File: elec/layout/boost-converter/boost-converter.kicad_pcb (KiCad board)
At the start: 2 copper layers, 14 parts

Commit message: build and re-link layouts
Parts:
- C7: value 4.7µF ±20% 6.3V X5R -> 4.7µF ±20% 10V X5R
- R1: value 10kΩ ±1% 62.5mW -> 10kΩ ±1% 100mW; footprint atopile:R0402-56259e -> atopile:R0603-ebcab9
- R2: value 180kΩ ±1% 62.5mW -> 180kΩ ±1% 100mW; footprint atopile:R0402-56259e -> atopile:R0603-ebcab9
- R3: value 2.7kΩ ±1% 62.5mW -> 2.49kΩ ±1% 62.5mW

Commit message: all modules building
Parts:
- C7: value 4.7µF ±20% 10V X5R -> 4.7µF ±20% 6.3V X5R
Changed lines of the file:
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@@
                     (size 1 1)
                     (thickness 0.15))))
-        (property "Value" "4.7µF ±20% 10V X5R"
+        (property "Value" "4.7µF ±20% 6.3V X5R"
             (at 0 4 90)
             (layer "F.Fab")
@@
                     (size 0.125 0.125)
                     (thickness 0.01875))))
-        (property "LCSC" "C23733"
+        (property "LCSC" "C307423"
             (at 0 0 90)
             (layer "User.9")
@@
                     (size 0.125 0.125)
                     (thickness 0.01875))))
-        (property "Partnumber" "CL05A475MP5NRNC"
+        (property "Partnumber" "CL05A475MQ5NRNC"
             (at 0 0 90)
             (layer "User.9")
@@
                     (size 0.125 0.125)
                     (thickness 0.01875))))
-        (property "JLCPCB description" "10V 4.7uF X5R ±20% 0402 Multilayer Ceramic Capacitors MLCC - SMD/SMT ROHS"
+        (property "JLCPCB description" "6.3V 4.7uF X5R ±20% 0402 Multilayer Ceramic Capacitors MLCC - SMD/SMT ROHS"
             (at 0 0 90)
             (layer "User.9")

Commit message: HIL Building
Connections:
- C2 pad 1: hv-1 -> hv
- C3 pad 1: hv-1 -> hv
- C4 pad 1: hv -> hv-1
- C5 pad 1: hv -> hv-1
- C6 pad 1: hv -> hv-1
- D1 pad 1: hv -> hv-1
- L1 pad 1: hv-1 -> hv
- R2 pad 1: hv -> hv-1
- U1 pad 2: hv-1 -> hv
- U1 pad 3: hv-1 -> hv
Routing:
- net hv-1: track 17.0 -> 14.5 mm, vias 5 -> 12
- net hv: track 14.5 -> 17.0 mm, vias 12 -> 5
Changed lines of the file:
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@@
     (net 2 "FB")
     (net 3 "ic.footprint.pins[5].net-net")
-    (net 4 "hv-1")
-    (net 5 "hv")
+    (net 4 "hv")
+    (net 5 "hv-1")
     (net 6 "net")
     (net 7 "SS")
@@
             (layers "F.Cu" "F.Paste" "F.Mask")
             (remove_unused_layers no)
-            (net 5 "hv")))
+            (net 5 "hv-1")))
     (footprint "atopile:R0603-ebcab9"
         (layer "F.Cu")
@@
             (layers "F.Cu" "F.Paste" "F.Mask")
             (remove_unused_layers no)
-            (net 4 "hv-1"))
+            (net 4 "hv"))
         (pad "2" smd rect
             (at 1 0 0)
@@
             (layers "F.Cu" "F.Paste" "F.Mask")
             (remove_unused_layers no)
-            (net 4 "hv-1"))
+            (net 4 "hv"))
         (pad "2" smd rect
             (at 1 0 0)
@@
             (layers "F.Cu" "F.Paste" "F.Mask")
             (remove_unused_layers no)
-            (net 5 "hv"))
+            (net 5 "hv-1"))
         (pad "2" smd rect
             (at 1 0 0)
@@
             (layers "F.Cu" "F.Paste" "F.Mask")
             (remove_unused_layers no)
-            (net 5 "hv"))
+            (net 5 "hv-1"))
         (pad "2" smd rect
             (at 1 0 0)
@@
                     (size 0.125 0.125)
                     (thickness 0.01875))))
-        (property "LCSC" "C137935"
+        (property "LCSC" "C25798"
             (at 0 0 90)
             (layer "User.9")
@@
                     (size 0.125 0.125)
                     (thickness 0.01875))))
-        (property "Partnumber" "RC0402FR-0775KL"
+        (property "Partnumber" "0402WGF7502TCE"
             (at 0 0 90)
             (layer "User.9")
@@
                     (size 0.125 0.125)
                     (thickness 0.01875))))
-        (property "Manufacturer" "YAGEO"
+        (property "Manufacturer" "UNI-ROYAL(Uniroyal Elec)"
             (at 0 0 90)
             (layer "User.9")
@@
             (layers "F.Cu" "F.Paste" "F.Mask")
             (remove_unused_layers no)
-            (net 4 "hv-1"))
+            (net 4 "hv"))
         (pad "3" smd rect
             (at 0.25 1.5 270)
@@
             (layers "F.Cu" "F.Paste" "F.Mask")
             (remove_unused_layers no)
-            (net 4 "hv-1"))
+            (net 4 "hv"))
         (pad "4" smd rect
             (at 0.75 1.5 270)
@@
             (layers "F.Cu" "F.Paste" "F.Mask")
             (remove_unused_layers no)
-            (net 5 "hv"))
+            (net 5 "hv-1"))
         (pad "2" smd rect
             (at 1 0 0)
@@
             (layers "F.Cu" "F.Paste" "F.Mask")
             (remove_unused_layers no)
-            (net 4 "hv-1"))
+            (net 4 "hv"))
         (pad "2" smd rect
             (at 2.91 0 90)
@@
             (layers "F.Cu" "F.Paste" "F.Mask")
             (remove_unused_layers no)
-            (net 5 "hv"))
+            (net 5 "hv-1"))
         (pad "2" smd rect
             (at 3.43 0 0)
@@
     (zone
         (net 5)
-        (net_name "hv")
+        (net_name "hv-1")
         (layers "F.Cu")
         (hatch edge 0.5)
@@
     (zone
         (net 5)
-        (net_name "hv")
+        (net_name "hv-1")
         (layers "F.Cu")
         (hatch edge 0.5)
@@
     (zone
         (net 4)
-        (net_name "hv-1")
+        (net_name "hv")
         (layers "F.Cu")
         (hatch edge 0.5)

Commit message: build with latest main
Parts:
- removed C1: 6.8nF ±10% 50V X7R, atopile:C0402-b3ef17
- removed C2, C3, C4, C5, C6: 10µF ±10% 25V X5R, atopile:C0805-3b2e55
- removed C7: 4.7µF ±20% 6.3V X5R, atopile:C0402-b3ef17
- removed D1: , atopile:SMC_L7.1-W6.2-LS8.1-RD-d9649d
- removed L1: , atopile:IND-SMD_L7.1-W6.6-48b69f
- removed R1: 10kΩ ±1% 100mW, atopile:R0603-ebcab9
- removed R2: 180kΩ ±1% 100mW, atopile:R0603-ebcab9
- removed R3: 2.49kΩ ±1% 62.5mW, atopile:R0402-56259e
- removed R4: 75kΩ ±1% 62.5mW, atopile:R0402-56259e
- removed U1: , atopile:VQFN-16_L3.0-W3.0-P0.50-BL-EP1.7-62c35a
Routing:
- net gnd: track 17.2 -> 0.00 mm, vias 19 -> 0
- net hv: track 17.0 -> 0.00 mm, vias 5 -> 0
- net hv-1: track 14.5 -> 0.00 mm, vias 12 -> 0
- net switching_node: track 13.2 -> 0.00 mm
- net FB: track 4.55 -> 0.00 mm
- net COMP: track 3.32 -> 0.00 mm
- net FREQ: track 2.01 -> 0.00 mm
- net net: track 1.30 -> 0.00 mm
- net SS: track 1.24 -> 0.00 mm
- removed copper zone on B.Cu, net gnd
- removed copper zone on F.Cu, net gnd
- removed copper zone on F.Cu, net hv
- removed copper zone on F.Cu, net hv-1
- removed copper zone on F.Cu, net switching_node

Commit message: building frozen
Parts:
- added C1: 6.8nF ±10% 50V X7R, atopile:C0402-b3ef17, F.Cu at (106.1, 57.8)
- added C2: 10µF ±10% 25V X5R, atopile:C0805-3b2e55, F.Cu at (101.9, 59.6)
- added C3: 10µF ±10% 25V X5R, atopile:C0805-3b2e55, F.Cu at (101.9, 57.6)
- added C4: 10µF ±10% 25V X5R, atopile:C0805-3b2e55, F.Cu at (104.2, 46.0)
- added C5: 10µF ±10% 25V X5R, atopile:C0805-3b2e55, F.Cu at (104.2, 48.0)
- added C6: 10µF ±10% 25V X5R, atopile:C0805-3b2e55, F.Cu at (104.2, 50.0)
- added C7: 4.7µF ±20% 6.3V X5R, atopile:C0402-b3ef17, F.Cu at (100.5, 54.8)
- added D1: , atopile:SMC_L7.1-W6.2-LS8.1-RD-d9649d, F.Cu at (97.0, 48.3)
- added L1: , atopile:IND-SMD_L7.1-W6.6-48b69f, F.Cu at (96.4, 55.7)
- added R1: 10kΩ ±1% 100mW, atopile:R0603-ebcab9, F.Cu at (107.0, 52.9)
- added R2: 180kΩ ±1% 100mW, atopile:R0603-ebcab9, F.Cu at (106.3, 55.2)
- added R3: 2.49kΩ ±1% 62.5mW, atopile:R0402-56259e, F.Cu at (106.2, 56.5)
- added R4: 75kΩ ±1% 62.5mW, atopile:R0402-56259e, F.Cu at (105.8, 52.9)
- added U1: , atopile:VQFN-16_L3.0-W3.0-P0.50-BL-EP1.7-62c35a, F.Cu at (103.1, 53.8)
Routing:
- net gnd: track 0.00 -> 17.2 mm, vias 0 -> 19
- net hv: track 0.00 -> 17.0 mm, vias 0 -> 5
- net hv-1: track 0.00 -> 14.5 mm, vias 0 -> 12
- net switching_node: track 0.00 -> 13.2 mm
- net FB: track 0.00 -> 4.55 mm
- net COMP: track 0.00 -> 3.32 mm
- net FREQ: track 0.00 -> 2.01 mm
- net net: track 0.00 -> 1.30 mm
- net SS: track 0.00 -> 1.24 mm
- added copper zone on B.Cu, net gnd
- added copper zone on F.Cu, net gnd
- added copper zone on F.Cu, net hv
- added copper zone on F.Cu, net hv-1
- added copper zone on F.Cu, net switching_node

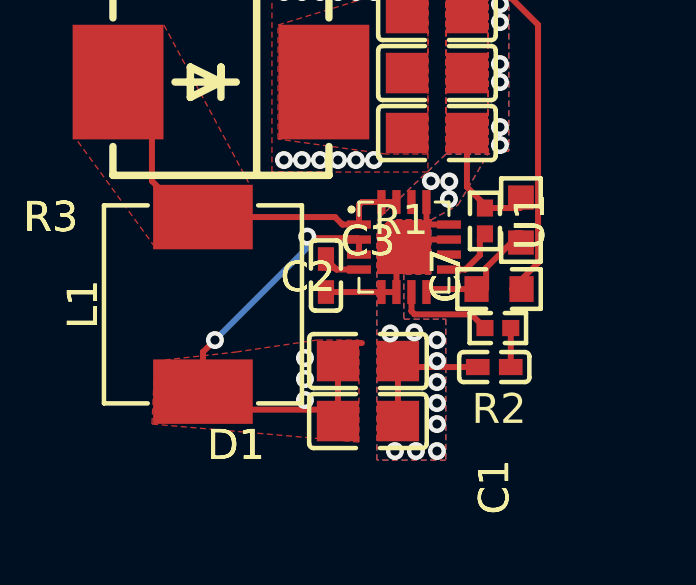
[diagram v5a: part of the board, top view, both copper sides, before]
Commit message: update layouts to kicad 9
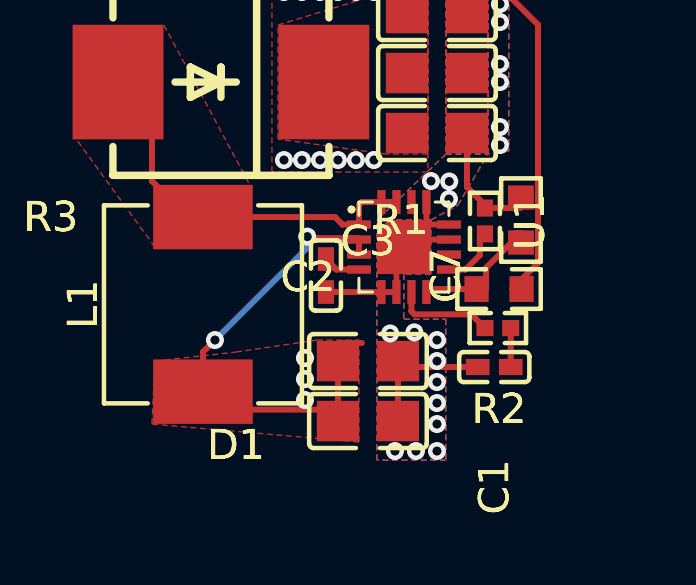
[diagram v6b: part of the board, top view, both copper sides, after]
